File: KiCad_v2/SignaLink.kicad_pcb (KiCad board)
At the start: 2 copper layers, 56.5 x 41.3 mm, 66 parts, among them Q1 MMBT3904, SW1 SW_Wake, U1 DM-OLED096-636, U2 ESP32-C3_SUPERMINI_TH, U3 MIC94063YC6-TR, U4 CM4102008, U5 LT8582EDKD-PBF, U6 MCP73871, U7 LM3940IMP-3.3, U8 BNO085, U9 MPU-6050

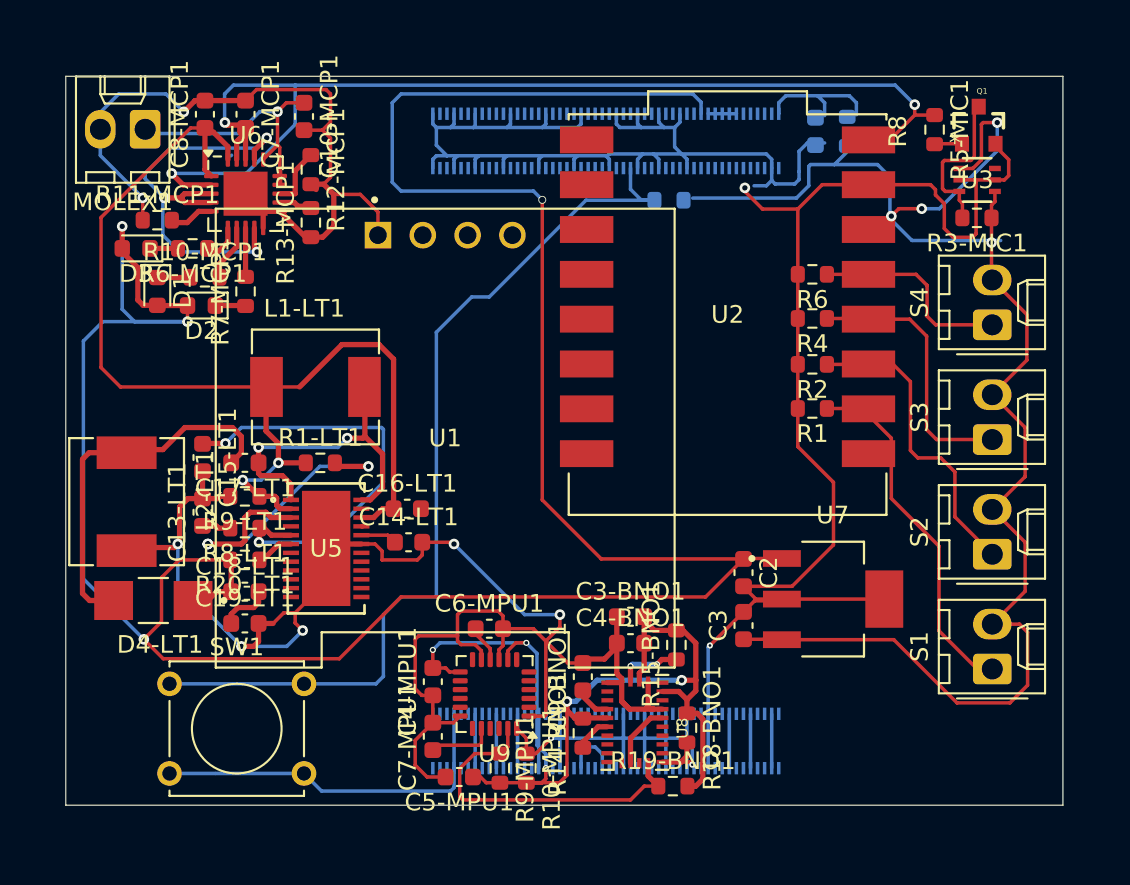
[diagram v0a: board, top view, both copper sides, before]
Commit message: feat: mas correcciones de pistas y tamaños
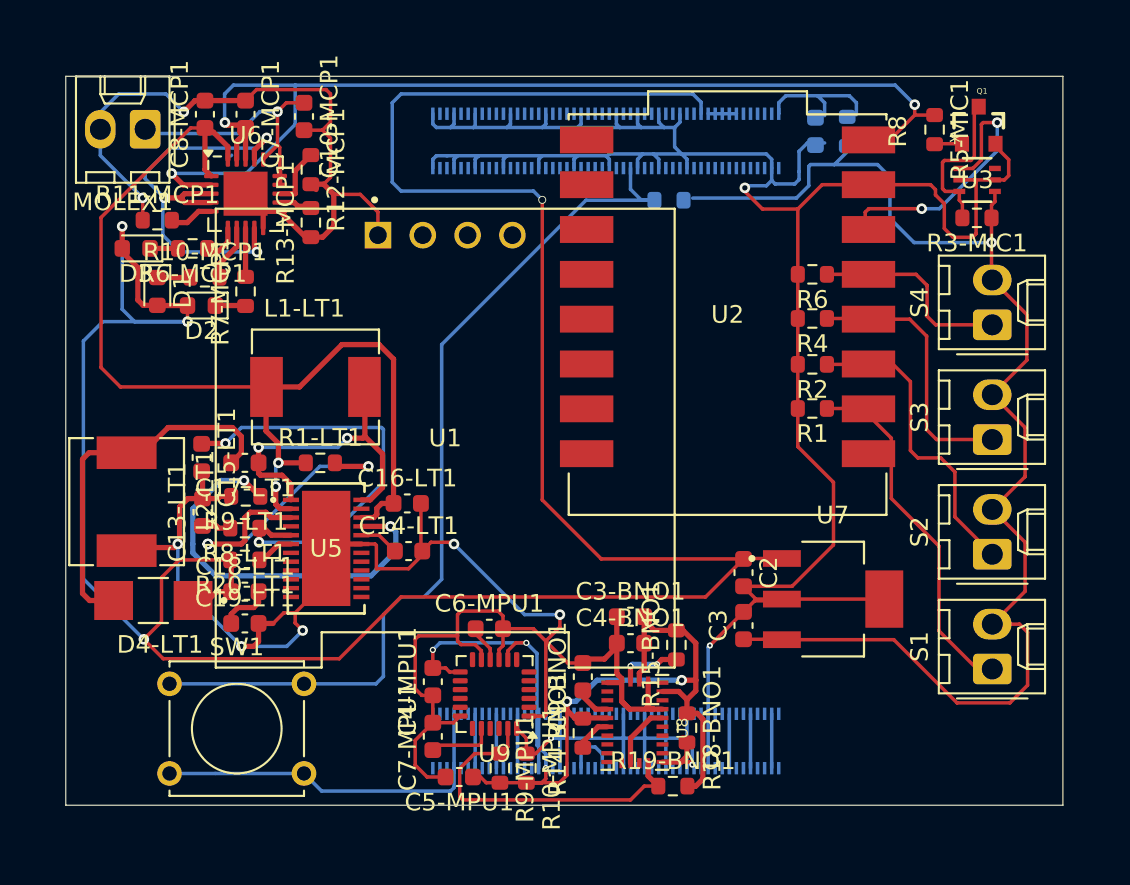
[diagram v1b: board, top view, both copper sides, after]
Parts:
- moved C14-LT1 0.50 mm to (39.9, 76.4)
- moved C16-LT1 0.30 mm to (39.9, 73.7)
- moved C15-LT1 0.05 mm to (28.2, 71.1)
- moved R9-LT1 0.05 mm to (30.7, 73.3)
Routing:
- net Net-(U5-RT1): track 0.14 -> 23.4 mm, vias 0 -> 2
- net GND: track 336.2 -> 341.0 mm
- net /power_supply/OUT_MCP: track 63.3 -> 60.7 mm
- net Net-(U4A-GPIO2): track 52.7 -> 51.7 mm
- net /MIC_OUT: track 15.6 -> 16.0 mm, vias 3 -> 2

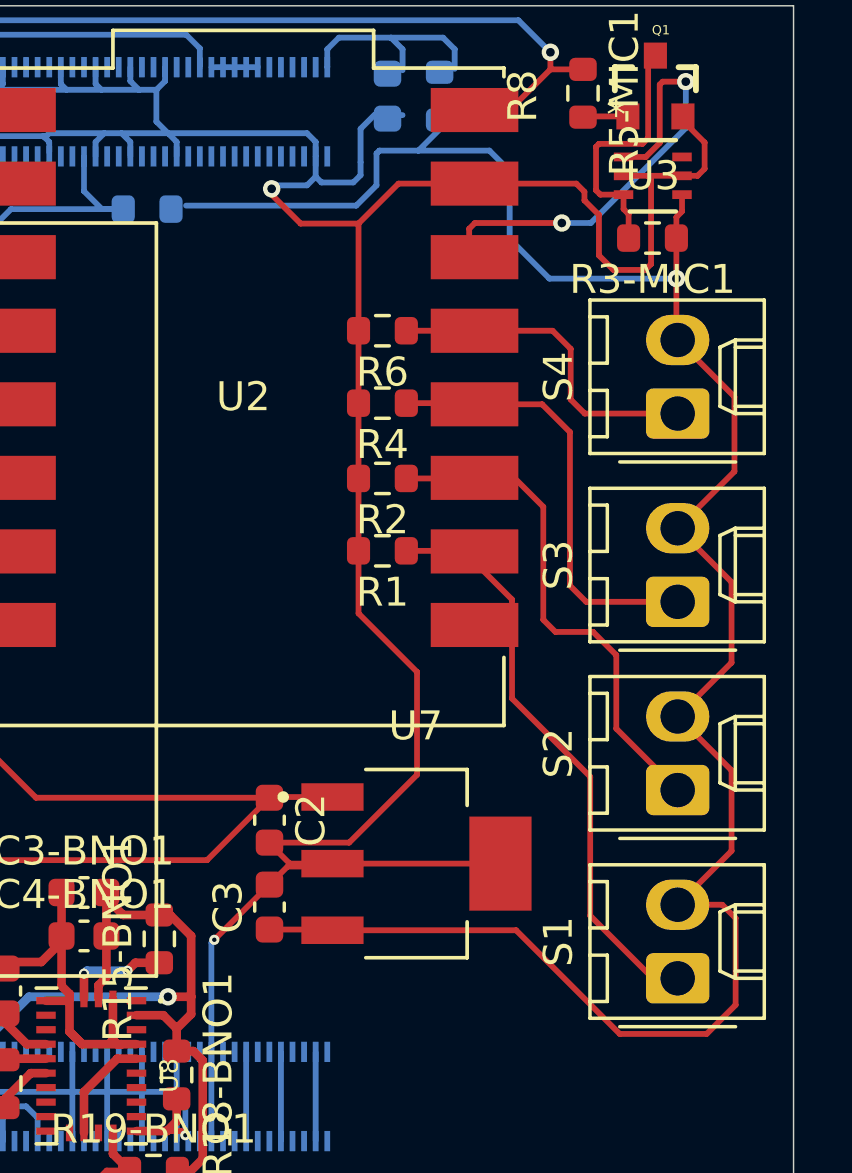
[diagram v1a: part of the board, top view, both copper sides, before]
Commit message: Falta conexion LCD
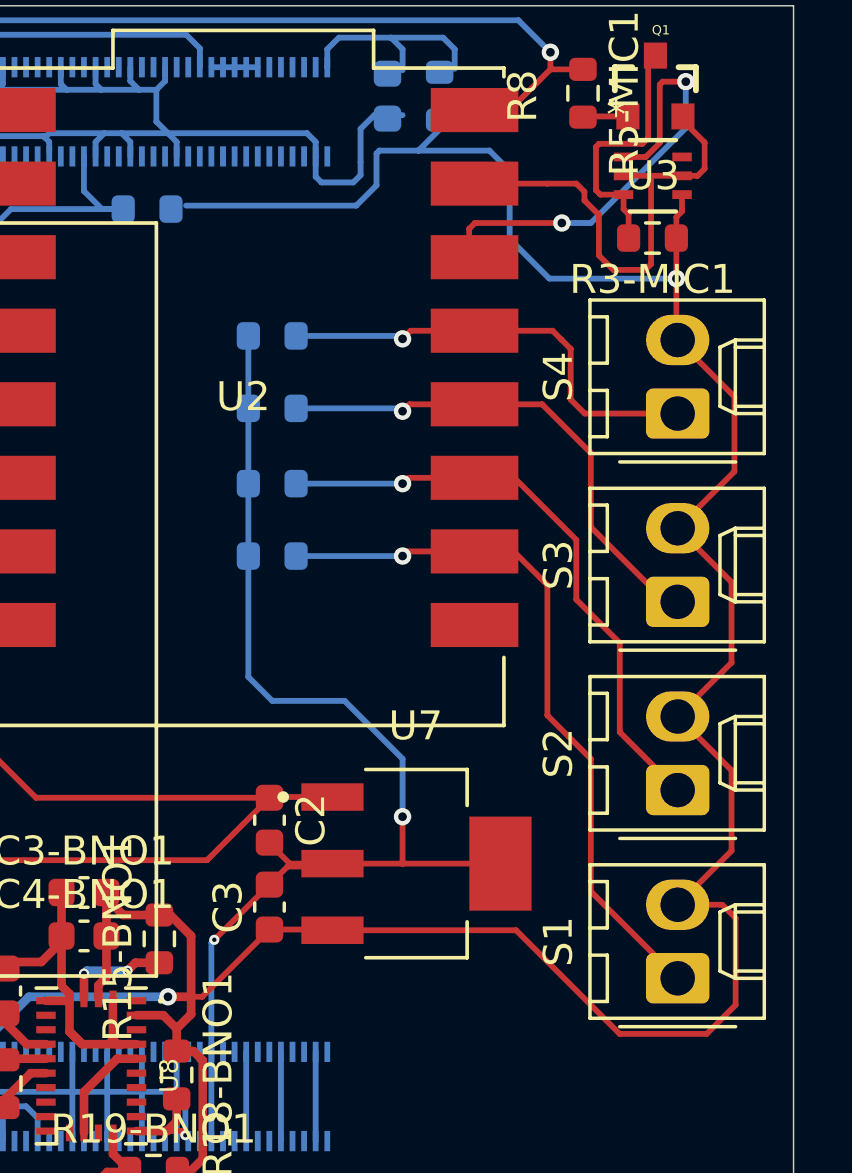
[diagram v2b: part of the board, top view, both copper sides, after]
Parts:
- R1, R2, R4, R6: moved to B.Cu
- moved R1 3.81 mm to (59.0, 68.5)
- moved R2 3.81 mm to (59.0, 66.0)
- moved R4 3.81 mm to (59.0, 63.4)
- moved R6 3.81 mm to (59.0, 60.9)
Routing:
- net GND: track 341.0 -> 327.6 mm
- net /A1: track 20.3 -> 25.6 mm, vias 0 -> 1
- net /A4: track 11.6 -> 16.1 mm, vias 0 -> 1
- net +3.3V: track 133.6 -> 137.3 mm
- net /A2: track 17.7 -> 21.2 mm, vias 0 -> 1
- net /A3: track 15.4 -> 18.1 mm, vias 0 -> 1

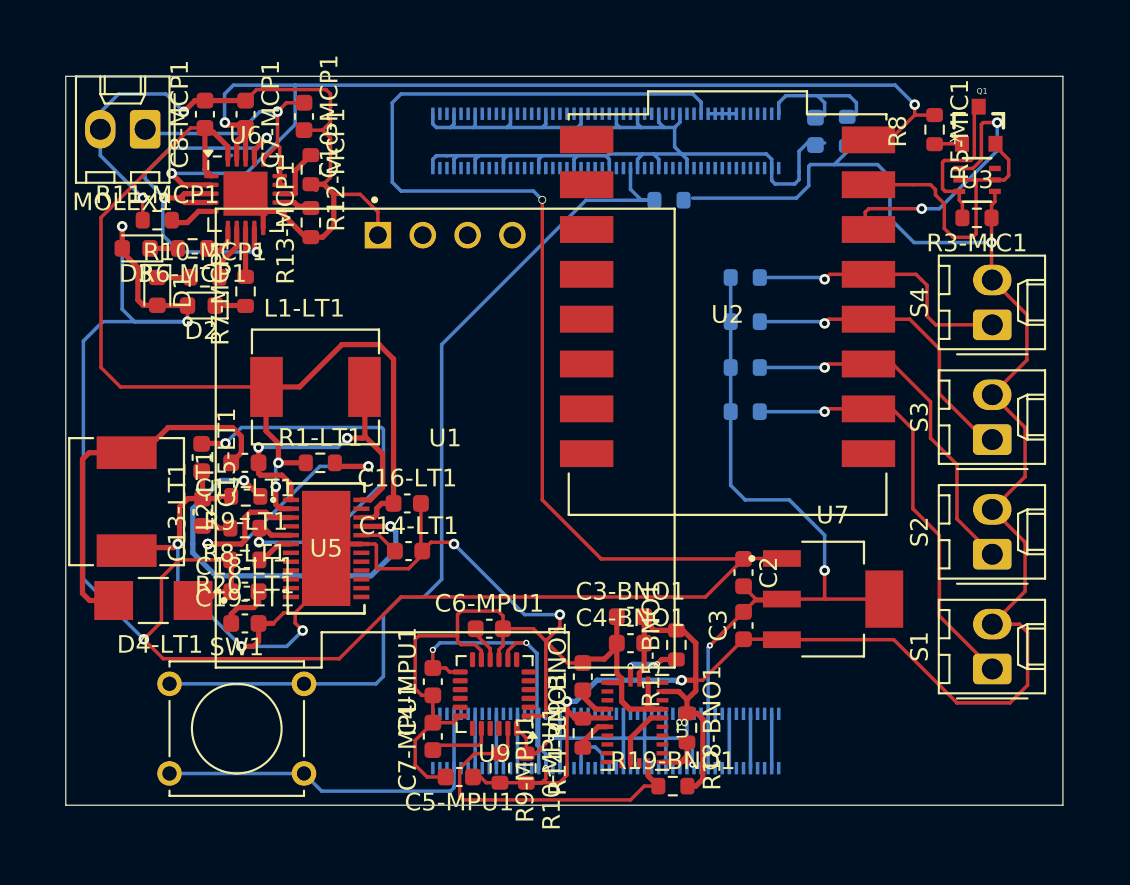
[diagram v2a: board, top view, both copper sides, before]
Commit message: conexiones de pistas
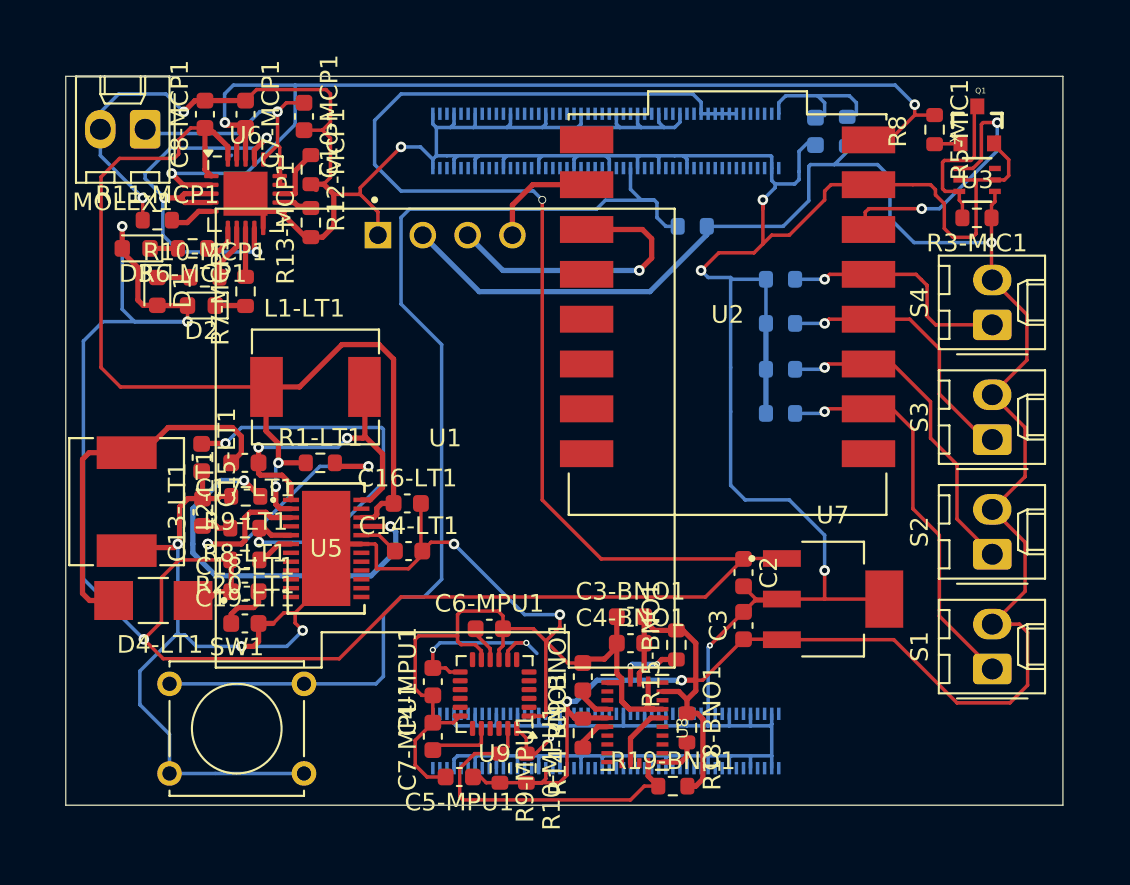
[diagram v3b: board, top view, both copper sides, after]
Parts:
- moved R4 2.00 mm to (61.0, 63.5)
- moved R6 2.00 mm to (61.0, 61.0)
- moved R1 2.00 mm to (61.0, 68.6)
- moved R2 2.00 mm to (61.0, 66.1)
- moved R7 1.98 mm to (56.0, 58.0)
- moved Q1 0.08 mm to (72.2, 52.3)
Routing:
- net GND: track 327.6 -> 371.5 mm, vias 9 -> 12
- net /SCL: track 19.1 -> 35.6 mm, vias 0 -> 1
- net +3.3V: track 137.3 -> 150.2 mm, vias 6 -> 5
- net Net-(U4A-GPIO2): track 51.7 -> 61.4 mm
- net /SDA: track 15.7 -> 12.1 mm, vias 2 -> 1
- net /A4: track 16.1 -> 14.1 mm
- net /A2: track 21.2 -> 19.3 mm
- net /A1: track 25.6 -> 23.6 mm
- net /A3: track 18.1 -> 16.2 mm
- net /power_supply/OUT_MCP: track 60.7 -> 62.6 mm
- net +5V: track 157.1 -> 158.3 mm

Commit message: Cambio grosor de pista de algunos componentes a 1mm
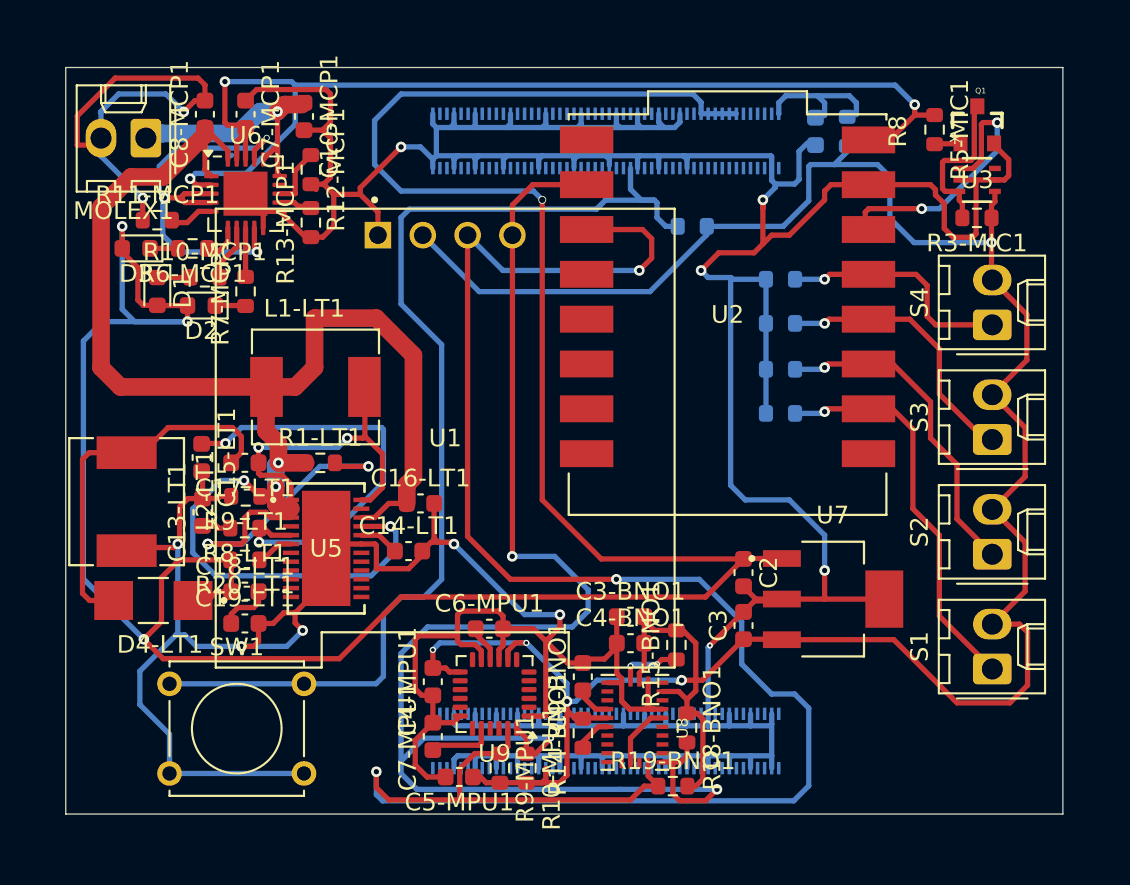
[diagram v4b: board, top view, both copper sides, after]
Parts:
- moved C16-LT1 0.75 mm to (40.6, 73.7)
- moved MOLEX1 0.50 mm to (25.0, 53.0)
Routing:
- net /SCL: track 35.6 -> 114.2 mm, vias 1 -> 3
- net /SDA: track 12.1 -> 87.1 mm, vias 1 -> 3
- net GND: track 371.5 -> 382.6 mm
- net +3.3V: track 150.2 -> 153.6 mm
- net /power_supply/OUT_MCP: track 62.6 -> 65.6 mm
- net /USB_PORT: track 64.4 -> 62.9 mm
- net /5V: track 25.1 -> 24.2 mm
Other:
- board size 56.5 x 41.3 mm -> 56.5 x 42.3 mm

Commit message: Cambio grosor de pista de algunos componentes a 1mm
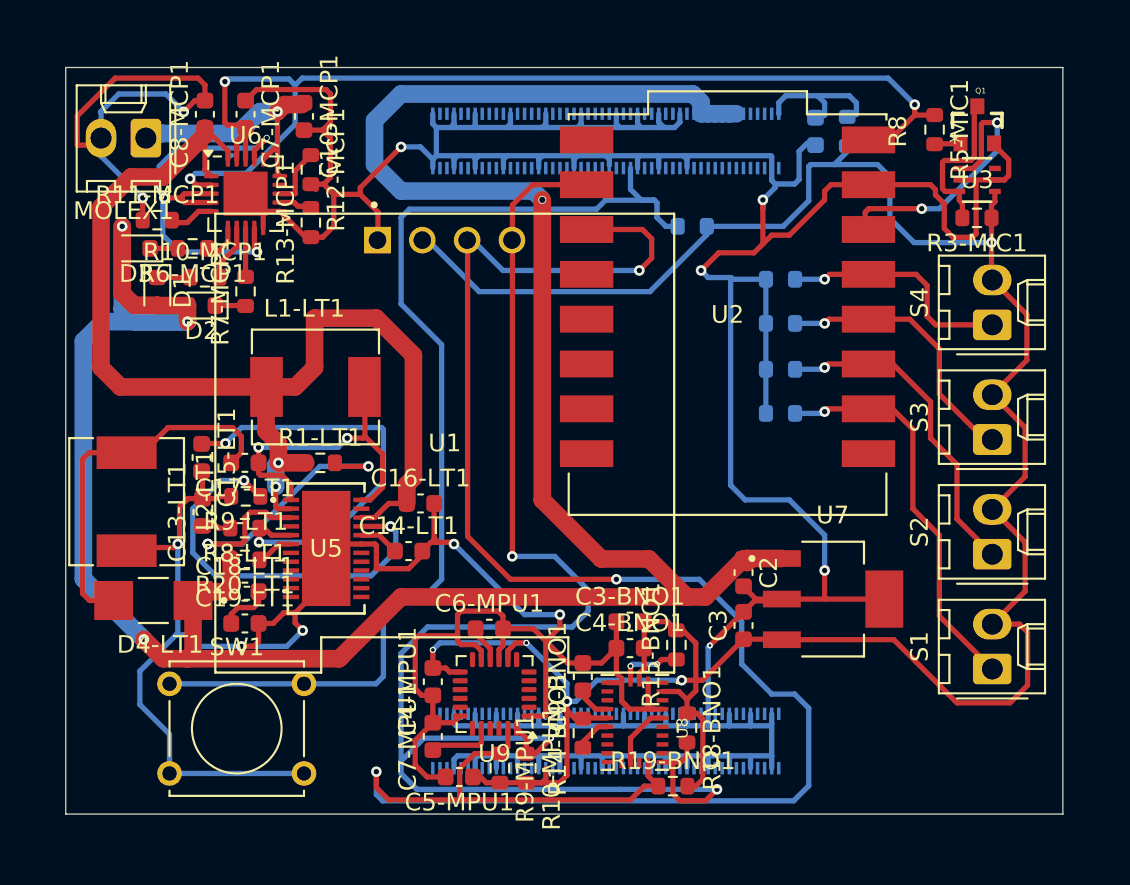
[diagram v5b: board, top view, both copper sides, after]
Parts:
- moved C3-BNO1 0.28 mm to (52.5, 80.4)
- moved C4-BNO1 0.28 mm to (52.5, 81.9)
- moved U1 0.28 mm to (42.0, 70.3)
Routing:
- net +5V: track 158.3 -> 151.2 mm

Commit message: pistas y vias arregladas
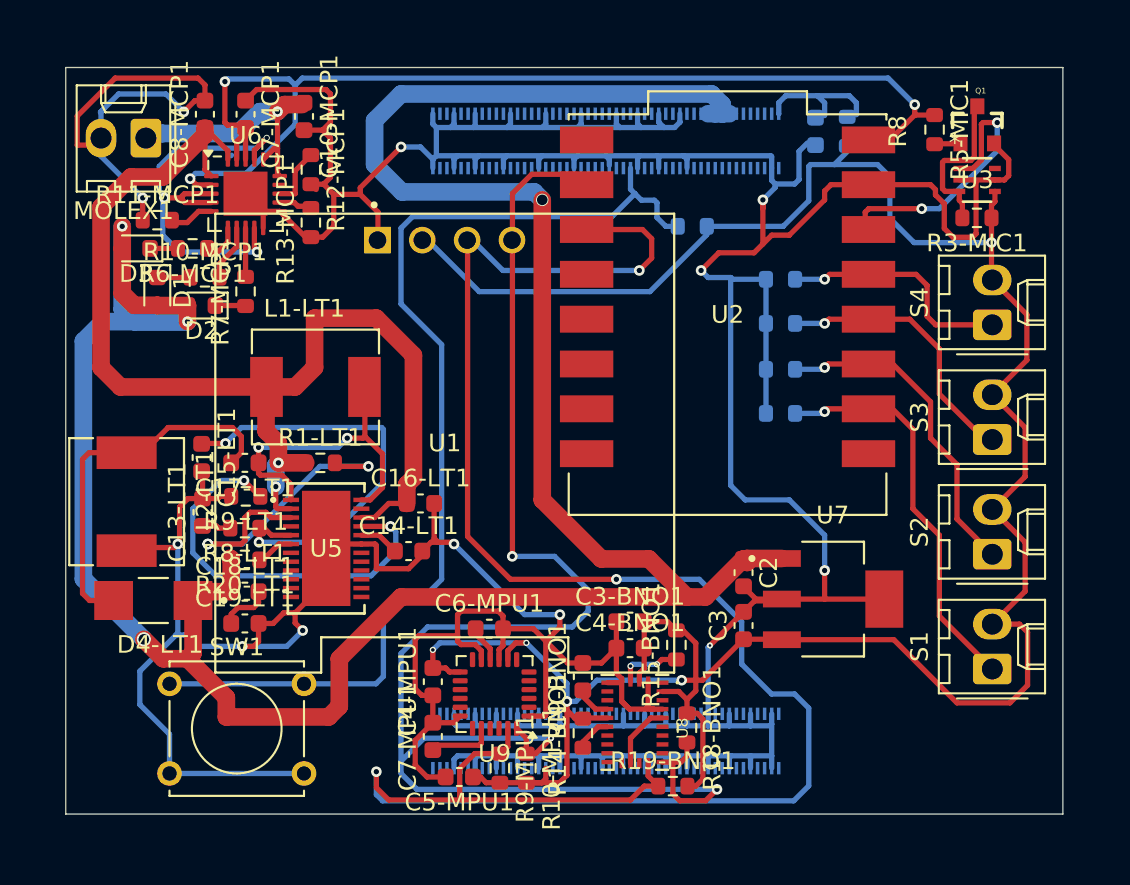
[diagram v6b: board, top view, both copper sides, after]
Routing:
- net +5V: track 151.2 -> 156.5 mm
- net GND: track 382.4 -> 383.8 mm
- net Net-(U4A-GPIO2): track 61.4 -> 60.1 mm
- net /SDA: track 87.1 -> 87.9 mm

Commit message: feat: arreglos en pistas y correcciones de errores
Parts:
- moved D2 0.23 mm to (28.4, 62.4)
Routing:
- net +5V: track 156.5 -> 148.4 mm, vias 4 -> 3
- net GND: track 383.8 -> 388.9 mm, vias 12 -> 13
- net +3.3V: track 153.6 -> 156.4 mm
- net /5V: track 24.2 -> 26.1 mm
- net /MIC_OUT: track 16.0 -> 17.4 mm
- net /A4: track 14.1 -> 13.0 mm
